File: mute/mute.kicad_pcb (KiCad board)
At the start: 2 copper layers, 54.6 x 38.1 mm, 24 parts, among them J1 AC sense, J2 tw in, J3 tw out, J4 w in, J5 w out, K1 G6S-2, Q1 npn, Q2 npn, Q3 pnp

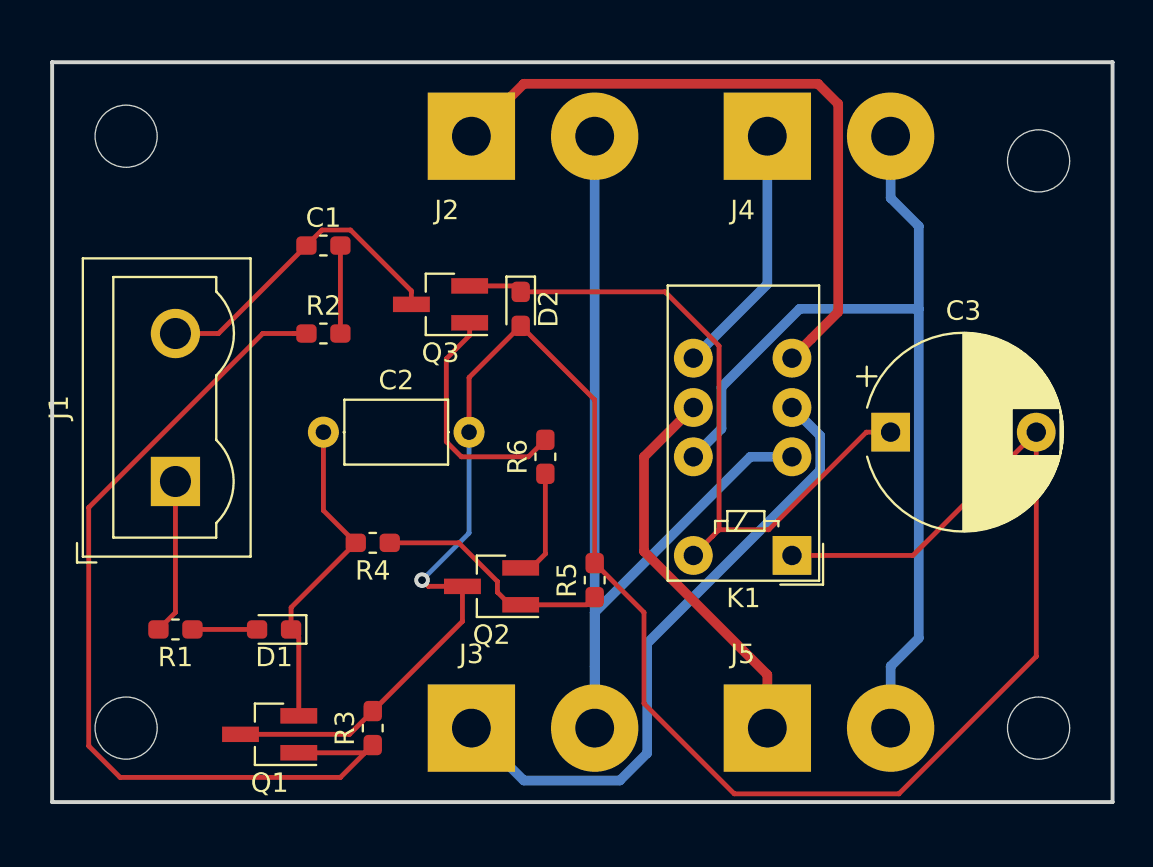
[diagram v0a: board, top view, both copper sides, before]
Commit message: Correct footprints
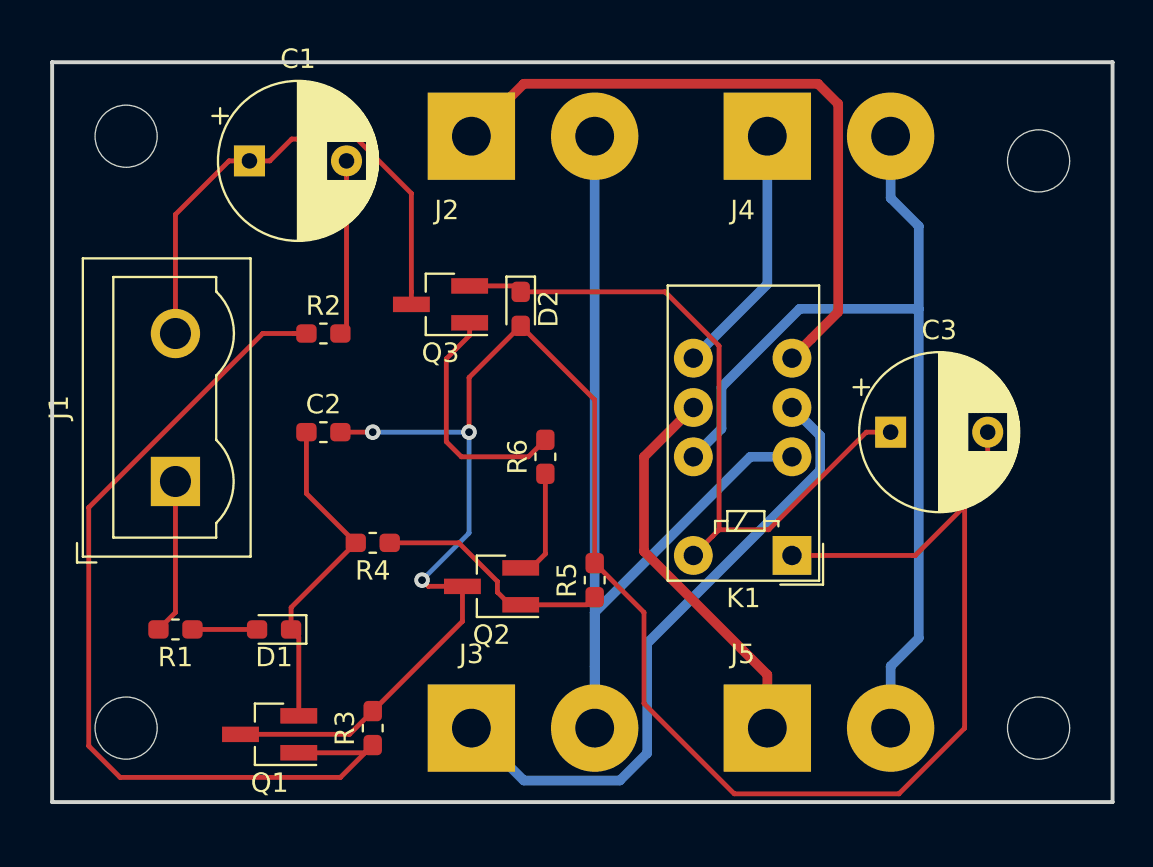
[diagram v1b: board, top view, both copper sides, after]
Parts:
- C1: footprint Capacitor_SMD:C_0603_1608Metric_Pad1.05x0.95mm_HandSolder -> Capacitor_THT:CP_Radial_D8.0mm_P5.00mm
- C2: footprint Capacitor_THT:C_Axial_L5.1mm_D3.1mm_P7.50mm_Horizontal -> Capacitor_SMD:C_0603_1608Metric_Pad1.05x0.95mm_HandSolder
- C3: value 1000u -> 100u; footprint Capacitor_THT:CP_Radial_D10.0mm_P7.50mm -> Capacitor_THT:CP_Radial_D8.0mm_P5.00mm
- moved C1 5.79 mm to (59.7, 85.1)
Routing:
- net Net-(C1-Pad1): track 16.4 -> 26.8 mm
- net Net-(C1-Pad2): track 4.53 -> 9.02 mm
- net GND: track 107.0 -> 107.3 mm, vias 1 -> 3

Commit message: Remove hifiberry-adc-dac, garduino untested
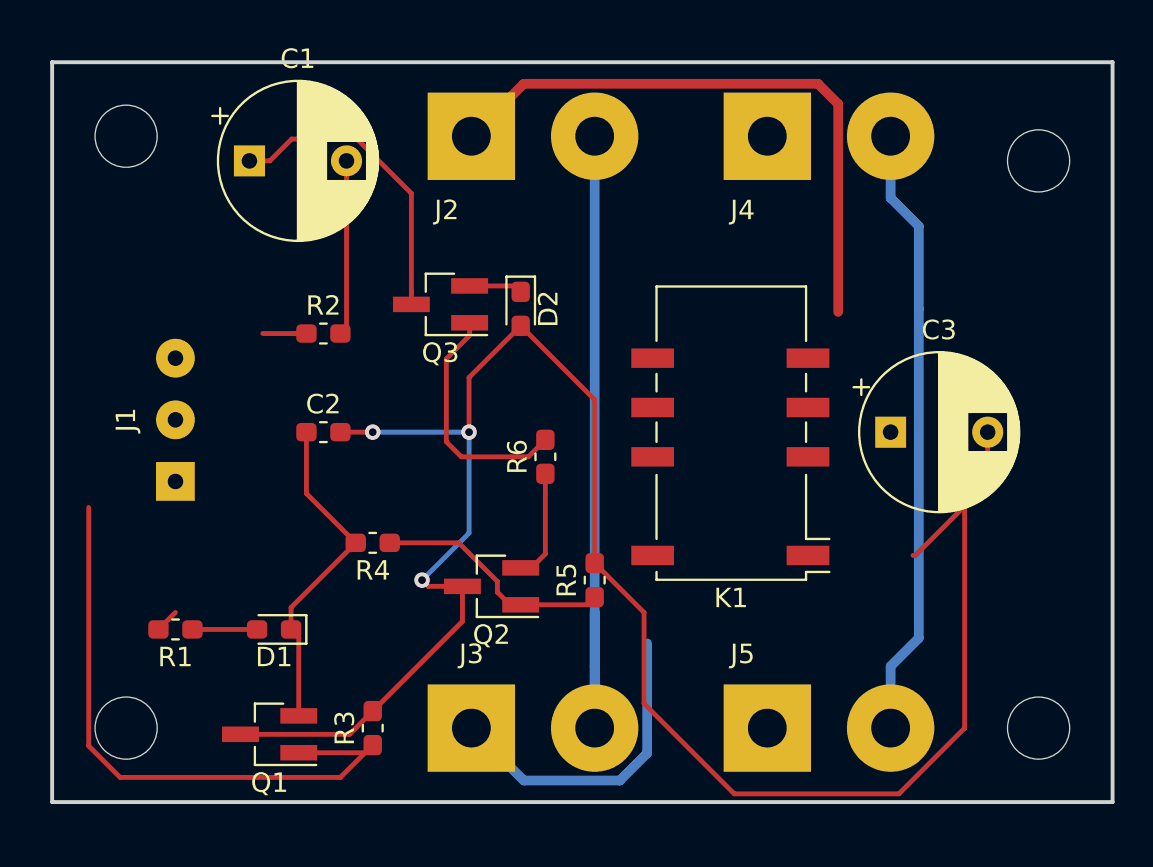
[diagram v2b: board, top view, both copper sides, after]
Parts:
- J1: value AC sense -> Conn_01x03; footprint TerminalBlock:TerminalBlock_Wuerth_691311400102_P7.62mm -> Connector_Wire:SolderWirePad_1x03_P3.175mm_Drill0.8mm
- K1: footprint Relay_THT:Relay_DPDT_Omron_G6S-2 -> Relay_SMD:Relay_DPDT_Omron_G6S-2F
- moved K1 7.10 mm to (84.5, 99.1)
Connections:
- J1 pad 1: /ACSense -> GND
- J1 pad 2: Net-(C1-Pad1) -> /ACSense
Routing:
- net /Aux: track 36.4 -> 2.76 mm
- net Net-(J5-Pad1): track 20.2 -> 0.00 mm
- net Net-(J3-Pad1): track 32.8 -> 16.4 mm
- net Net-(J4-Pad2): track 47.7 -> 31.7 mm
- net Net-(J2-Pad2): track 49.9 -> 36.4 mm
- net Net-(J4-Pad1): track 13.0 -> 0.00 mm
- net Net-(Q1-Pad1): track 47.2 -> 34.5 mm
- net Net-(C1-Pad1): track 26.8 -> 15.7 mm
- net /ACSense: track 7.98 -> 1.24 mm
- net GND: track 107.3 -> 101.0 mm
- net Net-(J2-Pad1): track 34.5 -> 31.2 mm

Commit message: Route mute, mostly automatic changes for peak-detect
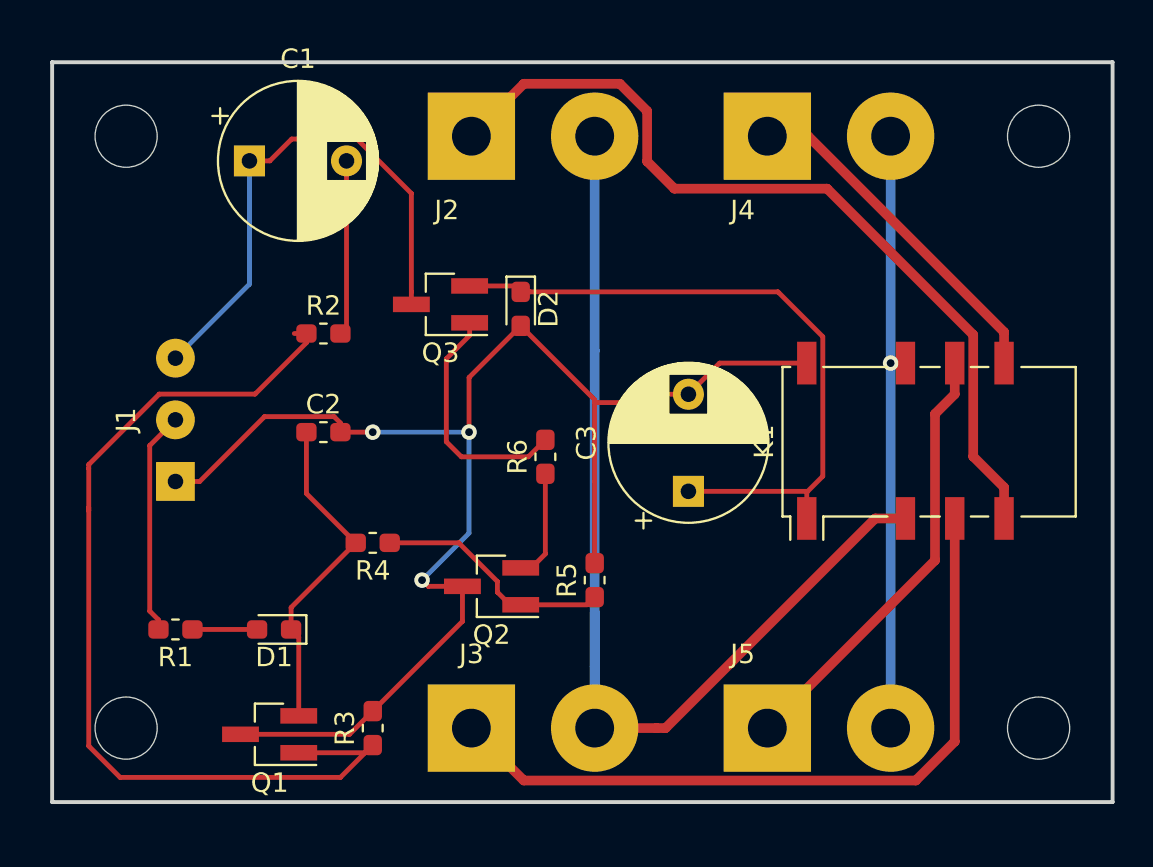
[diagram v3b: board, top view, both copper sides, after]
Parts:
- moved C3 10.9 mm to (82.3, 102.1), turned to 90 degrees
- moved K1 10.3 mm to (94.7, 99.5), turned to 90 degrees
- moved H3 1.27 mm to (100.3, 83.8)
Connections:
- K1 pad 1: GND -> /Aux
- K1 pad 10: /Aux -> Net-(J4-Pad2)
- K1 pad 8: Net-(J4-Pad2) -> Net-(J4-Pad1)
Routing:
- net /Aux: track 2.76 -> 35.4 mm
- net GND: track 101.0 -> 75.8 mm
- net Net-(J5-Pad1): track 0.00 -> 22.8 mm
- net Net-(J3-Pad1): track 16.4 -> 38.3 mm
- net Net-(J2-Pad2): track 36.4 -> 56.9 mm
- net Net-(J4-Pad1): track 0.00 -> 18.0 mm
- net Net-(Q1-Pad1): track 34.5 -> 49.5 mm
- net Net-(J2-Pad1): track 31.2 -> 44.0 mm
- net Net-(C1-Pad1): track 15.7 -> 27.4 mm
- net /ACSense: track 1.24 -> 11.5 mm
- net Net-(J4-Pad2): track 31.7 -> 31.2 mm, vias 0 -> 1

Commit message: Safer values, less power consumption
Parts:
- C1, C3: value 100u -> 1u
- R1: value 100 -> 10k
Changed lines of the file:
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@@
   )
   (setup
-    (last_trace_width 0.5)
+    (last_trace_width 0.25)
     (user_trace_width 0.5)
     (trace_clearance 0.2)
@@
       (effects (font (size 1 1) (thickness 0.15)))
     )
-    (fp_text value 100u (at 2.5 5.25 90) (layer F.Fab)
+    (fp_text value 1u (at 2.5 5.25 90) (layer F.Fab)
       (effects (font (size 1 1) (thickness 0.15)))
     )
@@
       (effects (font (size 1 1) (thickness 0.15)))
     )
-    (fp_text value 100 (at 0 1.43 180) (layer F.Fab)
+    (fp_text value 10k (at 0 1.43 180) (layer F.Fab)
       (effects (font (size 1 1) (thickness 0.15)))
     )
@@
       (effects (font (size 1 1) (thickness 0.15)))
     )
-    (fp_text value 100u (at 2.5 5.25) (layer F.Fab)
+    (fp_text value 1u (at 2.5 5.25) (layer F.Fab)
       (effects (font (size 1 1) (thickness 0.15)))
     )
@@
   (segment (start 64.04999 98.25999) (end 64.375 98.585) (width 0.25) (layer F.Cu) (net 4) (status 20))
   (segment (start 55.88 101.6) (end 57.12949 101.6) (width 0.25) (layer F.Cu) (net 4) (status 10))
-  (segment (start 88.312 95.504) (end 88.392 95.504) (width 0.25) (layer F.Cu) (net 4))
-  (segment (start 77.47 105.805) (end 77.47 101.6) (width 0.25) (layer F.Cu) (net 4))
+  (segment (start 88.312 95.504) (end 88.392 95.504) (width 0.25) (layer F.Cu) (net 4) (status 30))
+  (segment (start 77.47 105.805) (end 77.47 101.6) (width 0.25) (layer F.Cu) (net 4) (status 10))
   (segment (start 77.47 97.536) (end 77.47 97.395) (width 0.25) (layer F.Cu) (net 4))
   (segment (start 77.47 101.6) (end 77.47 97.536) (width 0.25) (layer F.Cu) (net 4))
-  (segment (start 83.9 95.504) (end 88.392 95.504) (width 0.25) (layer F.Cu) (net 4))
-  (segment (start 82.296 97.108) (end 83.9 95.504) (width 0.25) (layer F.Cu) (net 4))
+  (segment (start 83.9 95.504) (end 88.392 95.504) (width 0.25) (layer F.Cu) (net 4) (status 20))
+  (segment (start 82.296 97.108) (end 83.9 95.504) (width 0.25) (layer F.Cu) (net 4) (status 10))
   (segment (start 81.16463 97.108) (end 80.73663 97.536) (width 0.25) (layer F.Cu) (net 4))
   (segment (start 80.73663 97.536) (end 77.47 97.536) (width 0.25) (layer F.Cu) (net 4))
-  (segment (start 82.296 97.108) (end 81.16463 97.108) (width 0.25) (layer F.Cu) (net 4))
+  (segment (start 82.296 97.108) (end 81.16463 97.108) (width 0.25) (layer F.Cu) (net 4) (status 10))
   (segment (start 73.355 91.53) (end 73.66 91.835) (width 0.25) (layer F.Cu) (net 5) (status 30))
   (segment (start 71.03 91.53) (end 73.355 91.53) (width 0.25) (layer F.Cu) (net 5) (status 30))
-  (segment (start 73.66 91.835) (end 73.66 92.132002) (width 0.25) (layer F.Cu) (net 5))
+  (segment (start 73.66 91.835) (end 73.66 92.132002) (width 0.25) (layer F.Cu) (net 5) (status 30))
   (segment (start 88.346 102.108) (end 88.392 102.154) (width 0.25) (layer F.Cu) (net 5))
-  (segment (start 82.296 102.108) (end 88.346 102.108) (width 0.25) (layer F.Cu) (net 5))
-  (segment (start 74.135 91.835) (end 73.66 91.835) (width 0.25) (layer F.Cu) (net 5))
+  (segment (start 82.296 102.108) (end 88.346 102.108) (width 0.25) (layer F.Cu) (net 5) (status 10))
+  (segment (start 74.135 91.835) (end 73.66 91.835) (width 0.25) (layer F.Cu) (net 5) (status 20))
   (segment (start 89.217001 101.328999) (end 89.217001 94.143999) (width 0.25) (layer F.Cu) (net 5))
   (segment (start 88.392 102.154) (end 89.217001 101.328999) (width 0.25) (layer F.Cu) (net 5))
   (segment (start 86.908002 91.835) (end 74.135 91.835) (width 0.25) (layer F.Cu) (net 5))
   (segment (start 89.217001 94.143999) (end 86.908002 91.835) (width 0.25) (layer F.Cu) (net 5))
-  (segment (start 88.392 103.504) (end 88.392 102.154) (width 0.25) (layer F.Cu) (net 5))
+  (segment (start 88.392 103.504) (end 88.392 102.154) (width 0.25) (layer F.Cu) (net 5) (status 10))
   (segment (start 56.755 109.22) (end 60.085 109.22) (width 0.25) (layer F.Cu) (net 6) (status 30))
   (segment (start 54.555509 99.749491) (end 54.555509 108.276509) (width 0.25) (layer F.Cu) (net 7))
@@
   (segment (start 77.47 94.869) (end 77.47 114.3) (width 0.5) (layer B.Cu) (net 8) (status 20))
   (segment (start 77.47 83.82) (end 77.47 94.869) (width 0.5) (layer B.Cu) (net 8) (status 10))
-  (segment (start 80.652602 114.3) (end 77.47 114.3) (width 0.5) (layer F.Cu) (net 8))
+  (segment (start 80.652602 114.3) (end 77.47 114.3) (width 0.5) (layer F.Cu) (net 8) (status 20))
   (segment (start 91.915559 103.504) (end 81.119559 114.3) (width 0.5) (layer F.Cu) (net 8))
   (segment (start 81.119559 114.3) (end 80.652602 114.3) (width 0.5) (layer F.Cu) (net 8))
-  (segment (start 93.472 103.504) (end 91.915559 103.504) (width 0.5) (layer F.Cu) (net 8))
+  (segment (start 93.472 103.504) (end 91.915559 103.504) (width 0.5) (layer F.Cu) (net 8) (status 10))
   (segment (start 80.170441 82.523787) (end 78.766213 81.119559) (width 0.5) (layer F.Cu) (net 9))
   (segment (start 80.170441 85.116213) (end 80.170441 82.523787) (width 0.5) (layer F.Cu) (net 9))
@@
   (segment (start 81.574669 86.520441) (end 80.170441 85.116213) (width 0.5) (layer F.Cu) (net 9))
   (segment (start 96.962001 94.043999) (end 89.438443 86.520441) (width 0.5) (layer F.Cu) (net 9))
-  (segment (start 73.820441 81.119559) (end 71.12 83.82) (width 0.5) (layer F.Cu) (net 9))
+  (segment (start 73.820441 81.119559) (end 71.12 83.82) (width 0.5) (layer F.Cu) (net 9) (status 20))
   (segment (start 78.766213 81.119559) (end 73.820441 81.119559) (width 0.5) (layer F.Cu) (net 9))
   (segment (start 98.552 101.904) (end 96.962001 100.314001) (width 0.5) (layer F.Cu) (net 9))
   (segment (start 96.962001 100.314001) (end 96.962001 94.043999) (width 0.5) (layer F.Cu) (net 9))
-  (segment (start 98.552 103.504) (end 98.552 101.904) (width 0.5) (layer F.Cu) (net 9))
+  (segment (start 98.552 103.504) (end 98.552 101.904) (width 0.5) (layer F.Cu) (net 9) (status 10))
   (segment (start 94.006213 117.000441) (end 73.820441 117.000441) (width 0.5) (layer F.Cu) (net 10))
   (segment (start 96.012 114.994654) (end 94.006213 117.000441) (width 0.5) (layer F.Cu) (net 10))
-  (segment (start 73.820441 117.000441) (end 71.12 114.3) (width 0.5) (layer F.Cu) (net 10))
-  (segment (start 96.012 103.504) (end 96.012 114.994654) (width 0.5) (layer F.Cu) (net 10))
-  (segment (start 98.552 93.904) (end 98.552 95.504) (width 0.5) (layer F.Cu) (net 11))
-  (segment (start 88.468 83.82) (end 98.552 93.904) (width 0.5) (layer F.Cu) (net 11))
-  (segment (start 86.36 83.82) (end 88.468 83.82) (width 0.5) (layer F.Cu) (net 11))
-  (segment (start 93.472 95.504) (end 92.71 95.504) (width 0.5) (layer F.Cu) (net 12))
-  (segment (start 92.71 95.504) (end 92.71 114.3) (width 0.5) (layer B.Cu) (net 12))
+  (segment (start 73.820441 117.000441) (end 71.12 114.3) (width 0.5) (layer F.Cu) (net 10) (status 20))
+  (segment (start 96.012 103.504) (end 96.012 114.994654) (width 0.5) (layer F.Cu) (net 10) (status 10))
+  (segment (start 98.552 93.904) (end 98.552 95.504) (width 0.5) (layer F.Cu) (net 11) (status 20))
+  (segment (start 88.468 83.82) (end 98.552 93.904) (width 0.5) (layer F.Cu) (net 11) (status 10))
+  (segment (start 86.36 83.82) (end 88.468 83.82) (width 0.5) (layer F.Cu) (net 11) (status 30))
+  (segment (start 93.472 95.504) (end 92.71 95.504) (width 0.5) (layer F.Cu) (net 12) (status 10))
+  (segment (start 92.71 95.504) (end 92.71 114.3) (width 0.5) (layer B.Cu) (net 12) (status 20))
   (via (at 92.71 95.504) (size 0.8) (drill 0.4) (layers F.Cu B.Cu) (net 12))
-  (segment (start 92.71 83.82) (end 92.71 95.504) (width 0.5) (layer B.Cu) (net 12))
+  (segment (start 92.71 83.82) (end 92.71 95.504) (width 0.5) (layer B.Cu) (net 12) (status 10))
   (segment (start 65.645 115.57) (end 66.04 115.175) (width 0.25) (layer F.Cu) (net 13) (status 30))
   (segment (start 62.23 115.57) (end 65.645 115.57) (width 0.25) (layer F.Cu) (net 13) (status 30))
@@
   (segment (start 74.93 99.455) (end 74.055 100.33) (width 0.25) (layer F.Cu) (net 16) (status 10))
   (segment (start 96.012 97.104) (end 94.996 98.12) (width 0.5) (layer F.Cu) (net 17))
-  (segment (start 96.012 95.504) (end 96.012 97.104) (width 0.5) (layer F.Cu) (net 17))
-  (segment (start 94.996 105.664) (end 86.36 114.3) (width 0.5) (layer F.Cu) (net 17))
+  (segment (start 96.012 95.504) (end 96.012 97.104) (width 0.5) (layer F.Cu) (net 17) (status 10))
+  (segment (start 94.996 105.664) (end 86.36 114.3) (width 0.5) (layer F.Cu) (net 17) (status 20))
   (segment (start 94.996 98.12) (end 94.996 105.664) (width 0.5) (layer F.Cu) (net 17))
 )
